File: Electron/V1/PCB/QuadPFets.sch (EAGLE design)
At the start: 53 parts, among them Q1 BC817-40SMD, Q2 BC817-40SMD, Q3 BC817-40SMD, Q4 BC817-40SMD, U1 MOSFET-PCHANNEL-SOIC8SOIC8, U2 MOSFET-PCHANNEL-SOIC8SOIC8, U3 MOSFET-PCHANNEL-SOIC8SOIC8, U4 MOSFET-PCHANNEL-SOIC8SOIC8, U5 ELECTRONDUALNAMED

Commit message: Update to swap channel 4 onto A5 rather than A3 as A3 does not support PWM.
DirtyPCBs order updated.
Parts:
- removed SJ7: (no value), jumper:SJ
- added SJ9: (no value), jumper:SJ
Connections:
- net CHANNEL_4: now also SJ9.1; no longer SJ7.1
- net N$42: no longer SJ7.2
- net N$44: now also SJ9.2
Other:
- note added: "Note V1.1 N-Channel FETs used A3 for Channel 4"
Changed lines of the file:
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@@
 <part name="SJ5" library="jumper" deviceset="SJ" device=""/>
 <part name="SJ6" library="jumper" deviceset="SJ" device=""/>
-<part name="SJ7" library="jumper" deviceset="SJ" device=""/>
 <part name="SJ8" library="jumper" deviceset="SJ" device=""/>
 <part name="H3" library="holes" deviceset="MOUNT-HOLE" device="3.2" value="MOUNT-HOLE3.2"/>
@@
 <part name="GND17" library="SparkFun-Aesthetics" deviceset="DGND" device=""/>
 <part name="FRAME2" library="SparkFun-Aesthetics" deviceset="FRAME-LETTER" device=""/>
+<part name="SJ9" library="jumper" deviceset="SJ" device=""/>
 </parts>
 <sheets>
@@
 <text x="239.268" y="12.446" size="1.778" layer="97">1.0</text>
 <text x="165.862" y="16.764" size="1.778" layer="97">Stephen Harrison</text>
+<text x="86.36" y="139.7" size="1.27" layer="97">Note V1.1 N-Channel FETs used
+A3 for Channel 4
+</text>
 </plain>
 <instances>
@@
 <instance part="R1" gate="G$1" x="228.6" y="111.76" rot="R180"/>
 <instance part="GND11" gate="G$1" x="208.28" y="104.14"/>
-<instance part="SJ1" gate="1" x="106.68" y="129.54"/>
-<instance part="SJ2" gate="1" x="106.68" y="127"/>
-<instance part="SJ3" gate="1" x="106.68" y="124.46"/>
-<instance part="SJ4" gate="1" x="106.68" y="121.92"/>
-<instance part="SJ5" gate="1" x="149.86" y="142.24"/>
-<instance part="SJ6" gate="1" x="149.86" y="144.78"/>
-<instance part="SJ7" gate="1" x="106.68" y="144.78"/>
-<instance part="SJ8" gate="1" x="106.68" y="147.32"/>
+<instance part="SJ1" gate="1" x="106.68" y="129.54" smashed="yes">
+<attribute name="VALUE" x="104.14" y="125.73" size="1.778" layer="96"/>
+</instance>
+<instance part="SJ2" gate="1" x="106.68" y="127" smashed="yes">
+<attribute name="VALUE" x="104.14" y="123.19" size="1.778" layer="96"/>
+</instance>
+<instance part="SJ3" gate="1" x="106.68" y="124.46" smashed="yes">
+<attribute name="VALUE" x="104.14" y="120.65" size="1.778" layer="96"/>
+</instance>
+<instance part="SJ4" gate="1" x="106.68" y="121.92" smashed="yes">
+<attribute name="VALUE" x="104.14" y="118.11" size="1.778" layer="96"/>
+</instance>
+<instance part="SJ5" gate="1" x="149.86" y="142.24" smashed="yes">
+<attribute name="VALUE" x="147.32" y="138.43" size="1.778" layer="96"/>
+</instance>
+<instance part="SJ6" gate="1" x="149.86" y="144.78" smashed="yes">
+<attribute name="VALUE" x="147.32" y="140.97" size="1.778" layer="96"/>
+</instance>
+<instance part="SJ8" gate="1" x="106.68" y="147.32" smashed="yes">
+<attribute name="VALUE" x="104.14" y="143.51" size="1.778" layer="96"/>
+</instance>
 <instance part="H3" gate="G$1" x="200.66" y="129.54"/>
 <instance part="H4" gate="G$1" x="200.66" y="137.16"/>
@@
 <instance part="FRAME2" gate="G$1" x="0" y="5.08"/>
 <instance part="FRAME2" gate="V" x="147.32" y="5.08"/>
+<instance part="SJ9" gate="1" x="106.68" y="149.86" smashed="yes">
+<attribute name="VALUE" x="104.14" y="146.05" size="1.778" layer="96"/>
+</instance>
 </instances>
 <busses>
@@
 </segment>
 </net>
-<net name="N$42" class="0">
-<segment>
-<pinref part="U5" gate="G$1" pin="A3"/>
-<wire x1="116.84" y1="144.78" x2="111.76" y2="144.78" width="0.1524" layer="91"/>
-<pinref part="SJ7" gate="1" pin="2"/>
-</segment>
-</net>
 <net name="N$44" class="0">
 <segment>
 <pinref part="U5" gate="G$1" pin="A5"/>
-<wire x1="116.84" y1="149.86" x2="114.3" y2="149.86" width="0.1524" layer="91"/>
+<pinref part="SJ9" gate="1" pin="2"/>
+<wire x1="111.76" y1="149.86" x2="116.84" y2="149.86" width="0.1524" layer="91"/>
 </segment>
 </net>
@@
 <net name="CHANNEL_4" class="0">
 <segment>
-<pinref part="SJ7" gate="1" pin="1"/>
-<wire x1="101.6" y1="144.78" x2="99.06" y2="144.78" width="0.1524" layer="91"/>
-<label x="99.06" y="144.78" size="1.27" layer="95" rot="R180" xref="yes"/>
-</segment>
-<segment>
 <pinref part="SJ1" gate="1" pin="1"/>
 <wire x1="101.6" y1="129.54" x2="99.06" y2="129.54" width="0.1524" layer="91"/>
@@
 <label x="7.62" y="139.7" size="1.27" layer="95" rot="R90" xref="yes"/>
 <junction x="12.7" y="139.7"/>
+</segment>
+<segment>
+<pinref part="SJ9" gate="1" pin="1"/>
+<wire x1="101.6" y1="149.86" x2="99.06" y2="149.86" width="0.1524" layer="91"/>
+<label x="99.06" y="149.86" size="1.27" layer="95" rot="R180" xref="yes"/>
 </segment>
 </net>
@@
 </segment>
 </net>
+<net name="N$42" class="0">
+<segment>
+<pinref part="U5" gate="G$1" pin="A3"/>
+<wire x1="116.84" y1="144.78" x2="114.3" y2="144.78" width="0.1524" layer="91"/>
+</segment>
+</net>

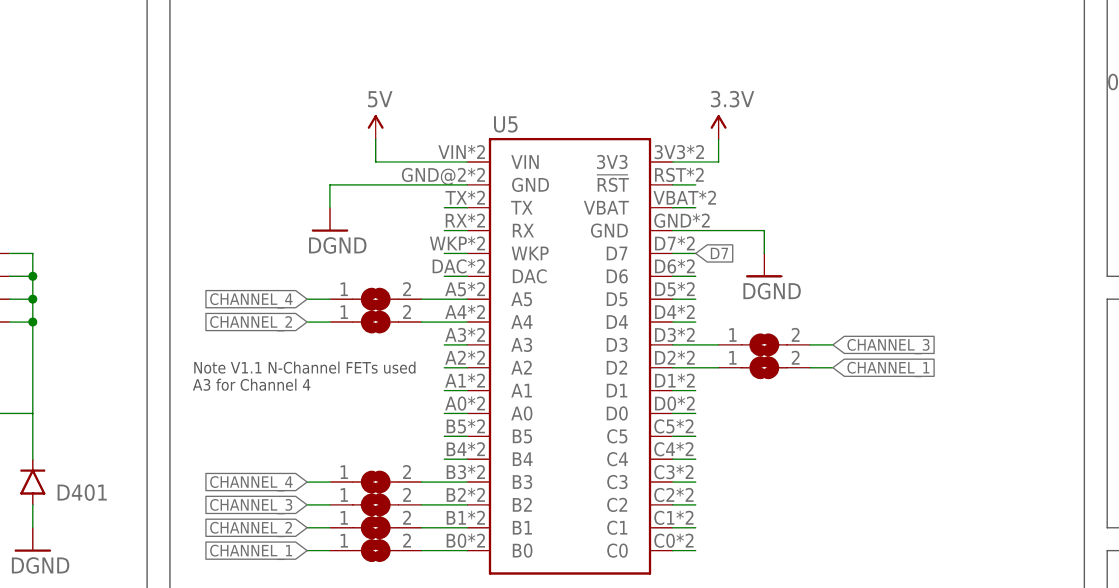
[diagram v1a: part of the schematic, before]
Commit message: Added more jumper options for PWM source (D0/D1 and TX/RX).
V1.0 order updated at DirtyPCBs
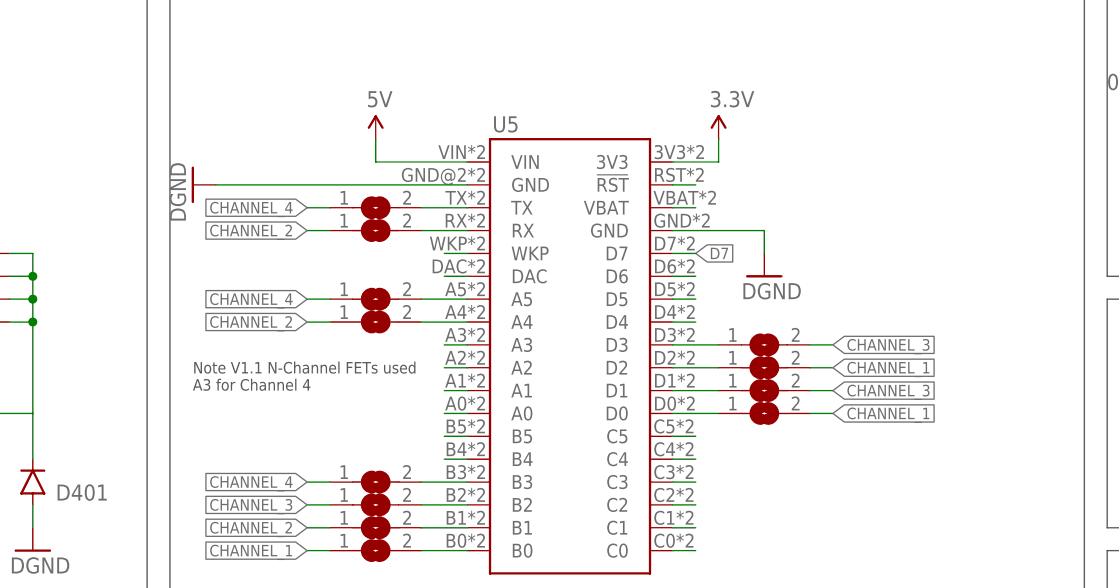
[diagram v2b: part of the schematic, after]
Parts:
- added SJ10, SJ11, SJ12, SJ7: (no value), jumper:SJ
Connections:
- net CHANNEL_1: now also SJ11.2
- net CHANNEL_2: now also SJ10.1
- net CHANNEL_3: now also SJ12.2
- net CHANNEL_4: now also SJ7.1
- net N$47: now also SJ10.2
- net N$48: now also SJ7.2
- net SCL: now also SJ12.1
- net SDA: now also SJ11.1
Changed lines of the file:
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@@
 <part name="FRAME2" library="SparkFun-Aesthetics" deviceset="FRAME-LETTER" device=""/>
 <part name="SJ9" library="jumper" deviceset="SJ" device=""/>
+<part name="SJ7" library="jumper" deviceset="SJ" device=""/>
+<part name="SJ10" library="jumper" deviceset="SJ" device=""/>
+<part name="SJ11" library="jumper" deviceset="SJ" device=""/>
+<part name="SJ12" library="jumper" deviceset="SJ" device=""/>
 </parts>
 <sheets>
@@
 <instance part="GND1" gate="G$1" x="210.82" y="157.48"/>
 <instance part="SUPPLY2" gate="G$1" x="106.68" y="167.64"/>
-<instance part="GND2" gate="G$1" x="101.6" y="157.48"/>
+<instance part="GND2" gate="G$1" x="86.36" y="162.56" rot="R270"/>
 <instance part="H1" gate="G$1" x="200.66" y="144.78"/>
 <instance part="SUPPLY4" gate="G$1" x="144.78" y="167.64"/>
@@
 <attribute name="VALUE" x="104.14" y="146.05" size="1.778" layer="96"/>
 </instance>
+<instance part="SJ7" gate="1" x="106.68" y="160.02" smashed="yes">
+<attribute name="VALUE" x="104.14" y="156.21" size="1.778" layer="96"/>
+</instance>
+<instance part="SJ10" gate="1" x="106.68" y="157.48" smashed="yes">
+<attribute name="VALUE" x="104.14" y="153.67" size="1.778" layer="96"/>
+</instance>
+<instance part="SJ11" gate="1" x="149.86" y="137.16" smashed="yes">
+<attribute name="VALUE" x="147.32" y="133.35" size="1.778" layer="96"/>
+</instance>
+<instance part="SJ12" gate="1" x="149.86" y="139.7" smashed="yes">
+<attribute name="VALUE" x="147.32" y="135.89" size="1.778" layer="96"/>
+</instance>
 </instances>
 <busses>
@@
 <pinref part="U5" gate="G$1" pin="GND@2"/>
 <pinref part="GND2" gate="G$1" pin="GND"/>
-<wire x1="116.84" y1="162.56" x2="101.6" y2="162.56" width="0.1524" layer="91"/>
-<wire x1="101.6" y1="162.56" x2="101.6" y2="160.02" width="0.1524" layer="91"/>
+<wire x1="116.84" y1="162.56" x2="88.9" y2="162.56" width="0.1524" layer="91"/>
 </segment>
 <segment>
@@
 <segment>
 <pinref part="U5" gate="G$1" pin="RX"/>
-<wire x1="116.84" y1="157.48" x2="114.3" y2="157.48" width="0.1524" layer="91"/>
+<pinref part="SJ10" gate="1" pin="2"/>
+<wire x1="111.76" y1="157.48" x2="116.84" y2="157.48" width="0.1524" layer="91"/>
 </segment>
 </net>
@@
 <segment>
 <pinref part="U5" gate="G$1" pin="TX"/>
-<wire x1="116.84" y1="160.02" x2="114.3" y2="160.02" width="0.1524" layer="91"/>
+<pinref part="SJ7" gate="1" pin="2"/>
+<wire x1="111.76" y1="160.02" x2="116.84" y2="160.02" width="0.1524" layer="91"/>
 </segment>
 </net>
@@
 <segment>
 <pinref part="U5" gate="G$1" pin="D0"/>
-<wire x1="139.7" y1="137.16" x2="142.24" y2="137.16" width="0.1524" layer="91"/>
+<pinref part="SJ11" gate="1" pin="1"/>
+<wire x1="144.78" y1="137.16" x2="139.7" y2="137.16" width="0.1524" layer="91"/>
 </segment>
 </net>
@@
 <segment>
 <pinref part="U5" gate="G$1" pin="D1"/>
-<wire x1="139.7" y1="139.7" x2="142.24" y2="139.7" width="0.1524" layer="91"/>
+<pinref part="SJ12" gate="1" pin="1"/>
+<wire x1="139.7" y1="139.7" x2="144.78" y2="139.7" width="0.1524" layer="91"/>
 </segment>
 </net>
@@
 <junction x="12.7" y="45.72"/>
 </segment>
+<segment>
+<pinref part="SJ11" gate="1" pin="2"/>
+<wire x1="154.94" y1="137.16" x2="157.48" y2="137.16" width="0.1524" layer="91"/>
+<label x="157.48" y="137.16" size="1.27" layer="95" xref="yes"/>
+</segment>
 </net>
 <net name="CHANNEL_2" class="0">
@@
 <wire x1="93.98" y1="43.18" x2="93.98" y2="45.72" width="0.1524" layer="91"/>
 <junction x="93.98" y="45.72"/>
+</segment>
+<segment>
+<pinref part="SJ10" gate="1" pin="1"/>
+<wire x1="101.6" y1="157.48" x2="99.06" y2="157.48" width="0.1524" layer="91"/>
+<label x="99.06" y="157.48" size="1.27" layer="95" rot="R180" xref="yes"/>
 </segment>
 </net>
@@
 <label x="99.06" y="149.86" size="1.27" layer="95" rot="R180" xref="yes"/>
 </segment>
+<segment>
+<pinref part="SJ7" gate="1" pin="1"/>
+<wire x1="101.6" y1="160.02" x2="99.06" y2="160.02" width="0.1524" layer="91"/>
+<label x="99.06" y="160.02" size="1.27" layer="95" rot="R180" xref="yes"/>
+</segment>
 </net>
 <net name="CHANNEL_3" class="0">
@@
 <junction x="17.78" y="93.98"/>
 </segment>
-</net>
+<segment>
+<pinref part="SJ12" gate="1" pin="2"/>
+<wire x1="154.94" y1="139.7" x2="157.48" y2="139.7" width="0.1524" layer="91"/>
+<label x="157.48" y="139.7" size="1.27" layer="95" xref="yes"/>
+</segment>
+</net>
